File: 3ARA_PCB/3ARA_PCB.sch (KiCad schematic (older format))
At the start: 74 parts, among them J1 ST-LINK V2, J10 Encoder 2, J11 Encoder 3, J12 JUMP_1, J13 JUMP_2, J14 I2C 1, J15 UART 5, J16 GPIO, J2 Motor 1, J3 Hall 3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

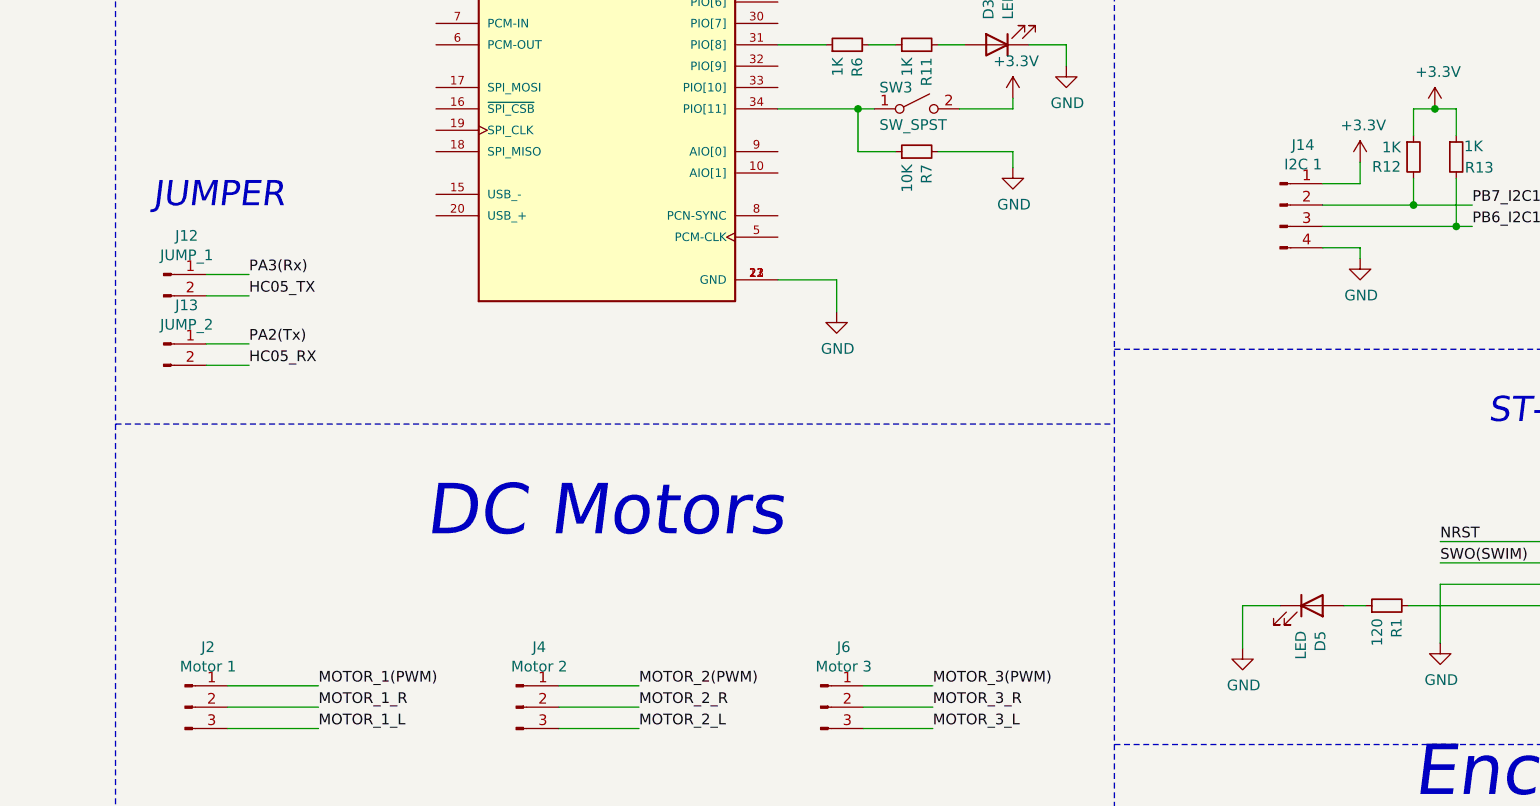
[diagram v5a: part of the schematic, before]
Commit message: Agregado de diseño 3D para HC05
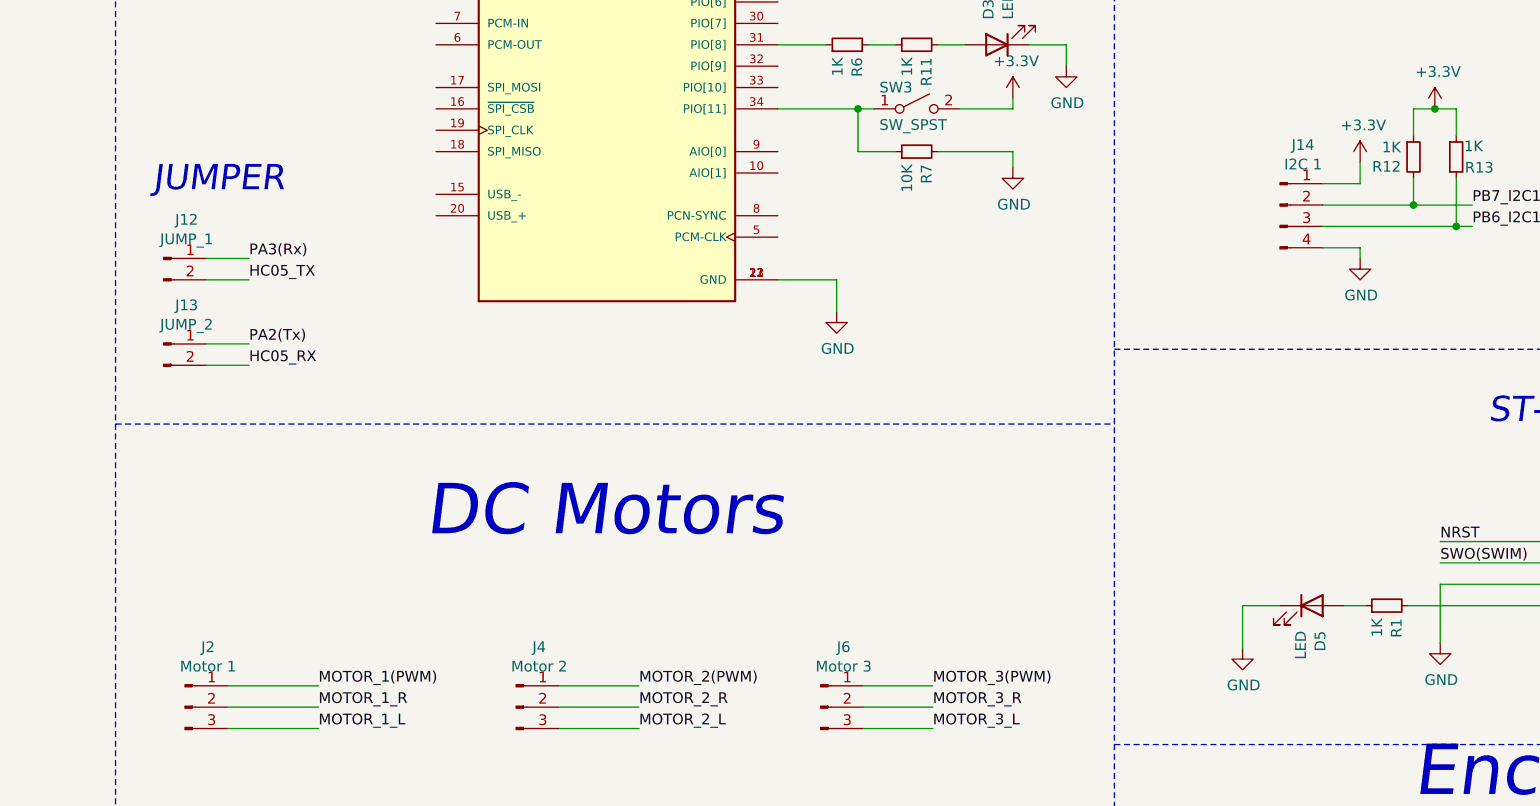
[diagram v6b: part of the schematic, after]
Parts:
- C21: footprint Capacitor_THT:CP_Radial_D10.0mm_P7.50mm -> Capacitor_THT:CP_Radial_D8.0mm_P3.50mm
- C3, C5: footprint Capacitor_THT:C_Disc_D5.0mm_W2.5mm_P5.00mm -> Capacitor_THT:C_Disc_D3.8mm_W2.6mm_P2.50mm
- D1, D6: footprint LED_SMD:LED_0805_2012Metric_Pad1.15x1.40mm_HandSolder -> LED_SMD:LED_1206_3216Metric_Pad1.42x1.75mm_HandSolder
- L2: footprint Inductor_THT:L_Axial_L7.0mm_D3.3mm_P12.70mm_Horizontal_Fastron_MICC -> Inductor_THT:L_Axial_L9.5mm_D4.0mm_P15.24mm_Horizontal_Fastron_SMCC
- R1: value 120 -> 1K
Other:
- moved on the sheet: J12
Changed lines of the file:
@@
 F 0 "C3" H 1400 3850 50  0000 L CNN
 F 1 "2.2uF" H 1325 3750 50  0000 L CNN
-F 2 "Capacitor_THT:C_Disc_D5.0mm_W2.5mm_P5.00mm" H 1338 3700 50  0001 C CNN
+F 2 "Capacitor_THT:C_Disc_D3.8mm_W2.6mm_P2.50mm" H 1338 3700 50  0001 C CNN
 F 3 "~" H 1300 3850 50  0001 C CNN
 	1    1300 3850
@@
 F 0 "C5" H 1775 3850 50  0000 L CNN
 F 1 "2.2uF" H 1700 3750 50  0000 L CNN
-F 2 "Capacitor_THT:C_Disc_D5.0mm_W2.5mm_P5.00mm" H 1713 3700 50  0001 C CNN
+F 2 "Capacitor_THT:C_Disc_D3.8mm_W2.6mm_P2.50mm" H 1713 3700 50  0001 C CNN
 F 3 "~" H 1675 3850 50  0001 C CNN
 	1    1675 3850
@@
 F 0 "D1" V 9914 1482 50  0000 R CNN
 F 1 "LED" V 9823 1482 50  0000 R CNN
-F 2 "LED_SMD:LED_0805_2012Metric_Pad1.15x1.40mm_HandSolder" H 9875 1600 50  0001 C CNN
+F 2 "LED_SMD:LED_1206_3216Metric_Pad1.42x1.75mm_HandSolder" H 9875 1600 50  0001 C CNN
 F 3 "~" H 9875 1600 50  0001 C CNN
 	1    9875 1600
@@
 Text Label 7325 6150 0    50   ~ 0
 PA2(Tx)
-Text Label 7325 5825 0    50   ~ 0
+Text Label 7325 5750 0    50   ~ 0
 PA3(Rx)
 $Comp
@@
 F 0 "C21" H 15168 2696 50  0000 L CNN
 F 1 "1000uF" H 15168 2605 50  0000 L CNN
-F 2 "Capacitor_THT:CP_Radial_D10.0mm_P7.50mm" H 15088 2500 50  0001 C CNN
+F 2 "Capacitor_THT:CP_Radial_D8.0mm_P3.50mm" H 15088 2500 50  0001 C CNN
 F 3 "~" H 15050 2650 50  0001 C CNN
 	1    15050 2650
@@
 L Connector:Conn_01x02_Male J12
 U 1 1 614571BD
-P 6925 5825
-F 0 "J12" H 7033 6006 50  0000 C CNN
-F 1 "JUMP_1" H 7033 5915 50  0000 C CNN
-F 2 "Connector_PinHeader_2.54mm:PinHeader_1x02_P2.54mm_Vertical" H 6925 5825 50  0001 C CNN
-F 3 "~" H 6925 5825 50  0001 C CNN
-	1    6925 5825
+P 6925 5750
+F 0 "J12" H 7033 5931 50  0000 C CNN
+F 1 "JUMP_1" H 7033 5840 50  0000 C CNN
+F 2 "Connector_PinHeader_2.54mm:PinHeader_1x02_P2.54mm_Vertical" H 6925 5750 50  0001 C CNN
+F 3 "~" H 6925 5750 50  0001 C CNN
+	1    6925 5750
 	1    0    0    -1
 $EndComp
@@
 	7675 4350 8200 4350
 Wire Wire Line
-	7125 5825 7325 5825
-Wire Wire Line
-	7325 5925 7125 5925
-Text Label 7325 5925 0    50   ~ 0
+	7125 5750 7325 5750
+Wire Wire Line
+	7325 5850 7125 5850
+Text Label 7325 5850 0    50   ~ 0
 HC05_TX
 Text Label 7325 6250 0    50   ~ 0
@@
 Wire Wire Line
 	7125 6250 7325 6250
-Text Notes 6875 5525 0    118  Italic 0
+Text Notes 6875 5450 0    118  Italic 0
 JUMPER
 $Comp
@@
 F 0 "L2" H 14550 2390 50  0000 C CNN
 F 1 "100uH - optional" H 14550 2299 50  0000 C CNN
-F 2 "Inductor_THT:L_Axial_L7.0mm_D3.3mm_P12.70mm_Horizontal_Fastron_MICC" H 14550 2175 50  0001 C CNN
+F 2 "Inductor_THT:L_Axial_L9.5mm_D4.0mm_P15.24mm_Horizontal_Fastron_SMCC" H 14550 2175 50  0001 C CNN
 F 3 "~" H 14550 2175 50  0001 C CNN
 	1    14550 2175
@@
 P 12650 7375
 F 0 "R1" H 12591 7329 50  0000 R CNN
-F 1 "120" H 12591 7420 50  0000 R CNN
+F 1 "1K" H 12591 7420 50  0000 R CNN
 F 2 "Resistor_SMD:R_0805_2012Metric_Pad1.20x1.40mm_HandSolder" H 12650 7375 50  0001 C CNN
 F 3 "~" H 12650 7375 50  0001 C CNN
@@
 F 0 "D6" V 15739 2632 50  0000 R CNN
 F 1 "LED" V 15648 2632 50  0000 R CNN
-F 2 "LED_SMD:LED_0805_2012Metric_Pad1.15x1.40mm_HandSolder" H 15700 2750 50  0001 C CNN
+F 2 "LED_SMD:LED_1206_3216Metric_Pad1.42x1.75mm_HandSolder" H 15700 2750 50  0001 C CNN
 F 3 "~" H 15700 2750 50  0001 C CNN
 	1    15700 2750
